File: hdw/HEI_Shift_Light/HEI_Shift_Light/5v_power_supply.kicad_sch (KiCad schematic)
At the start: 17 parts

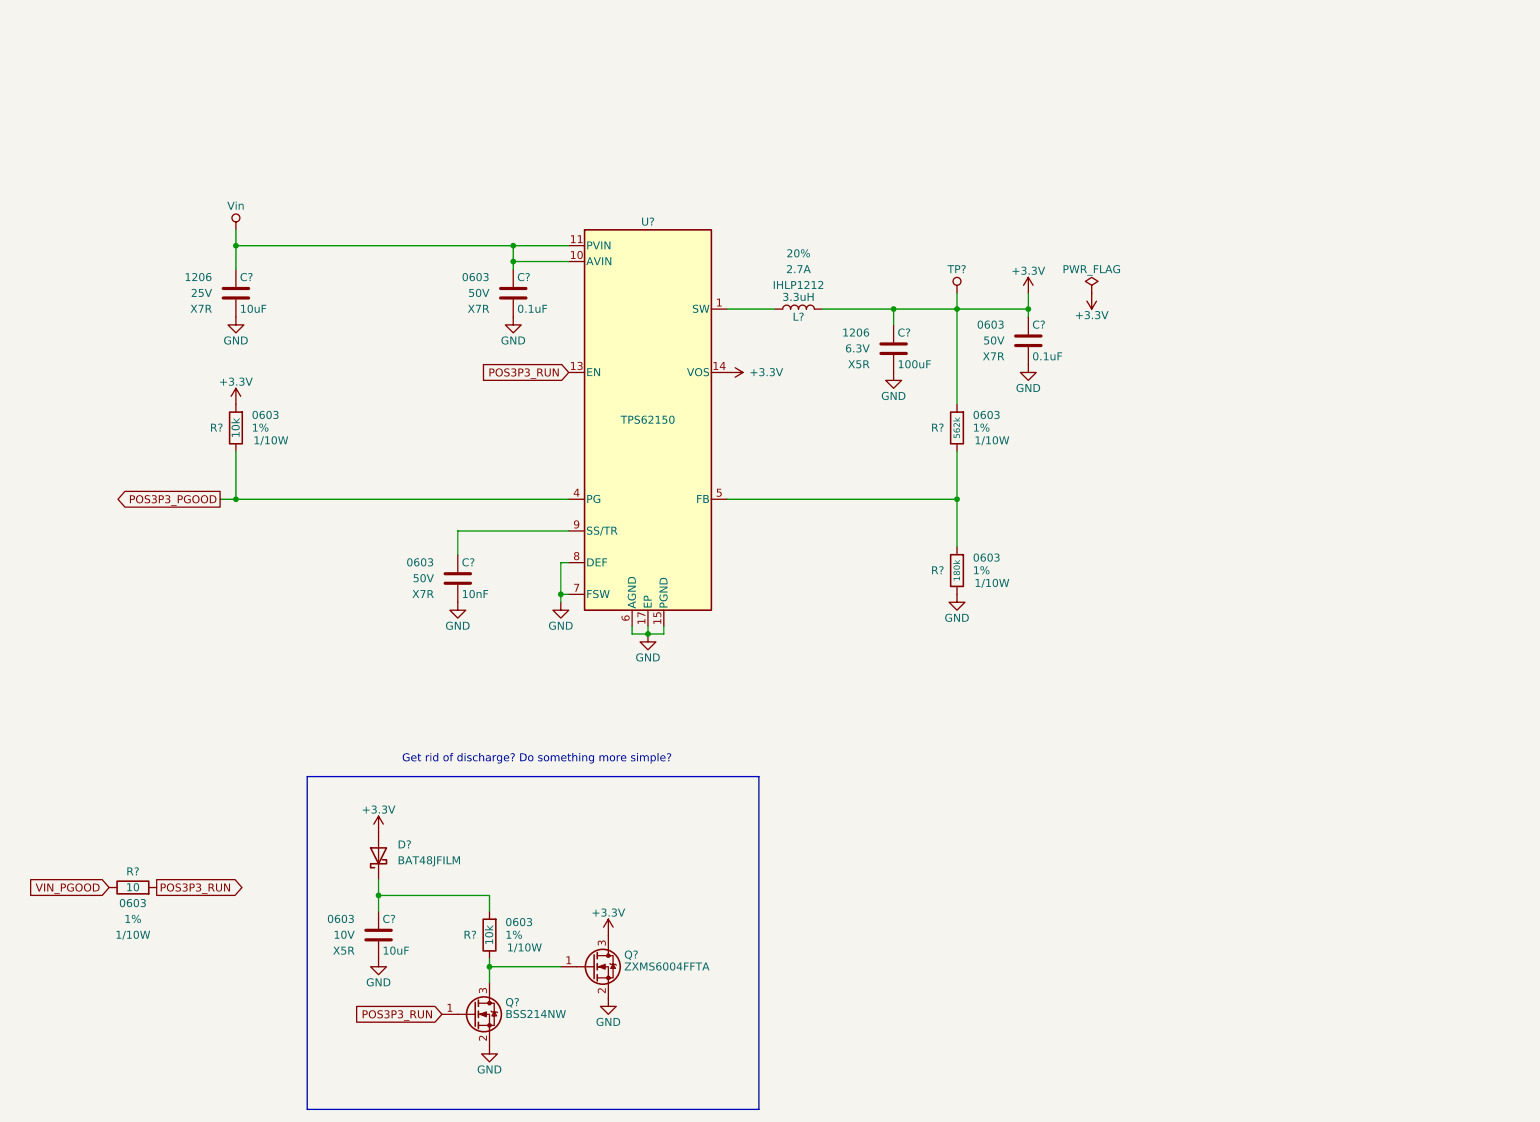
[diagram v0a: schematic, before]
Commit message: populated input protection circuit passive components, updated PIC pinout, added stuff to frequency to voltage converter circuit
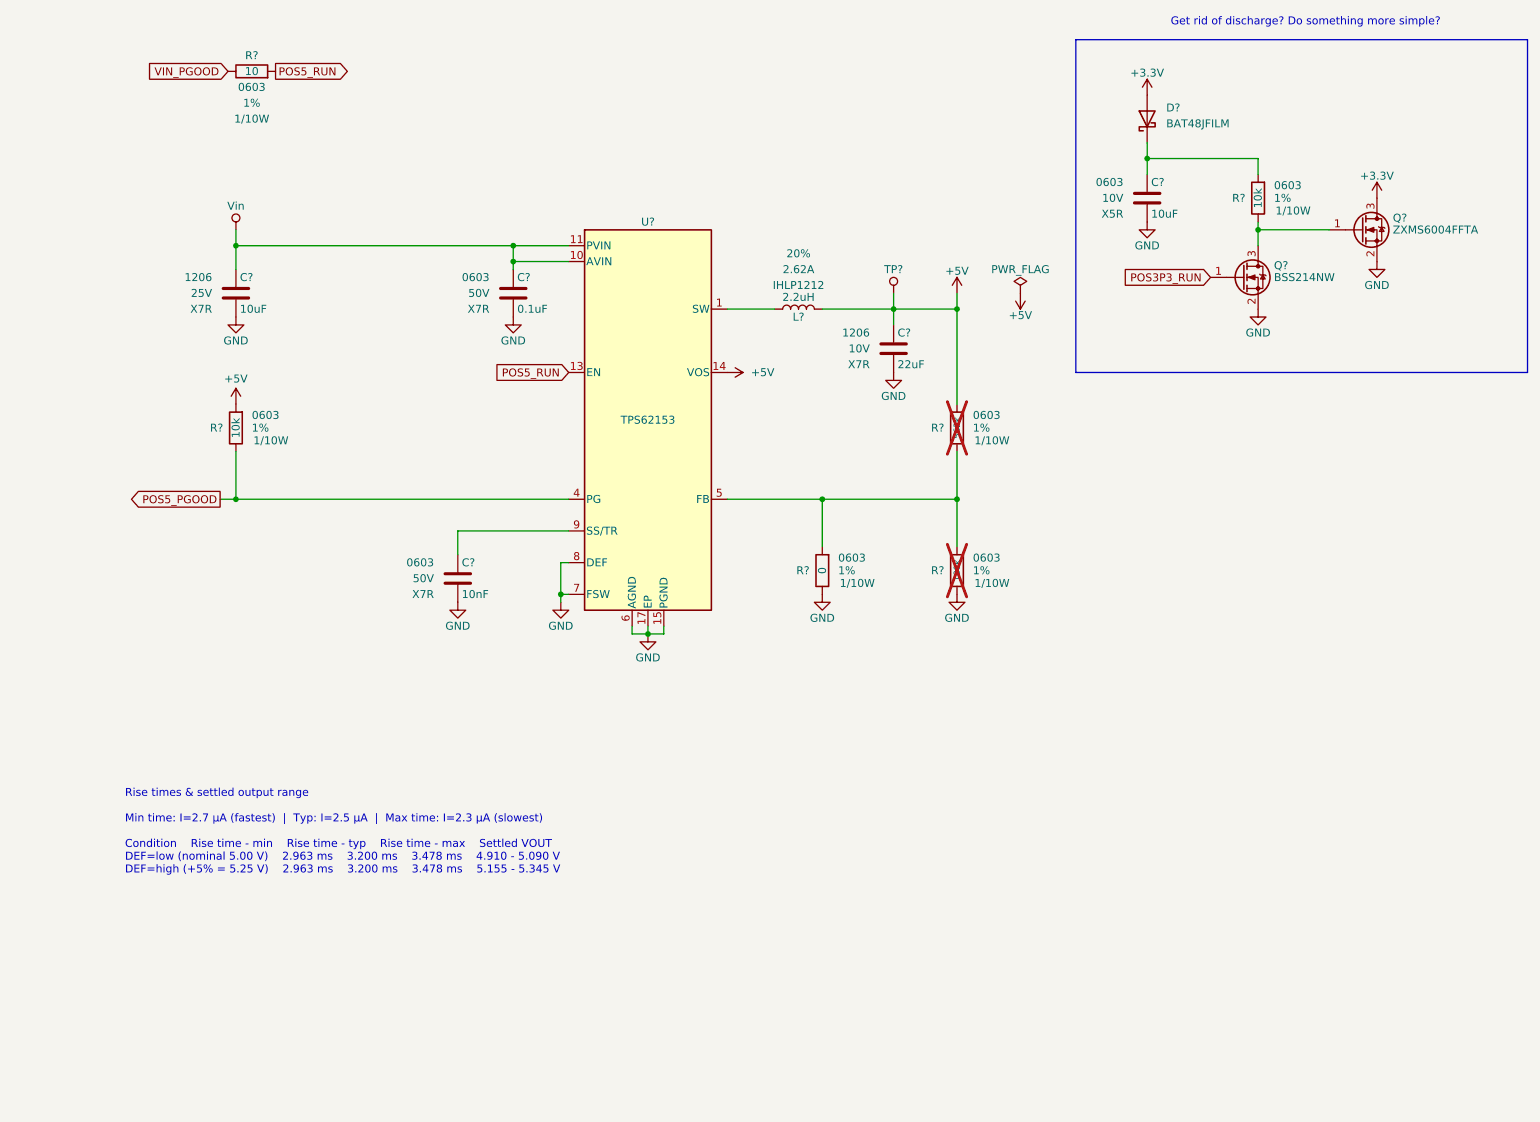
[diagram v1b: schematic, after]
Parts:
- removed C?: 0.1uF, Capacitors_SMD:C_0603, symbol Custom_Library:C_Custom
- added R?: 0, Resistors_SMD:R_0603, symbol Custom_Library:R_Custom
- C?: value 100uF -> 22uF; footprint Capacitors_SMD:C_1206 -> (none); Dielectric X5R -> X7R; Digi-Key PN 587-1963-1-ND -> (none); Voltage 6.3V -> 10V
- L?: value 3.3uH -> 2.2uH; Ampacity 2.7A -> 2.62A; Digi-Key PN 541-2567-1-ND -> 541-IHLP1212BZEV2R2M5ACT-ND
- R? (x2): now not fitted
- U?: value TPS62150 -> TPS62153; Digi-Key PN 296-41757-1-ND -> (none)
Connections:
- net +3.3V: no longer C?.1, L?.2, R?.1, R?.1, TP?.1 (TP), U?.14 (VOS)
- net GND: now also R?.2
- net POS3P3_RUN: no longer R?.1, U?.13 (EN)
- net at R?.1, R?.2, U?.5 (FB): now also R?.1
- net POS3P3_PGOOD renamed POS5_PGOOD
- new net +5V: C?.1, L?.2, R?.1, R?.1, TP?.1 (TP), U?.14 (VOS)
- new net POS5_RUN: R?.1, U?.13 (EN)
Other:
- note added: "Rise times & settled output range Min time: I=2.7 µA (fastest) | Typ: I=2.5 µA | Max time: I=2.3 µA (slowest) Condition Rise time - min Rise time - typ Rise time - max Settled VOUT DEF=low (nominal 5.00 V) 2.963 ms 3.200 ms 3.478 ms 4.910 - 5.090 V DEF=high (+5% = 5.25 V) 2.963 ms 3.200 ms 3.478 ms 5.155 - 5.345 V"
- moved on the sheet: C?, D?, Q?, R?, TP?

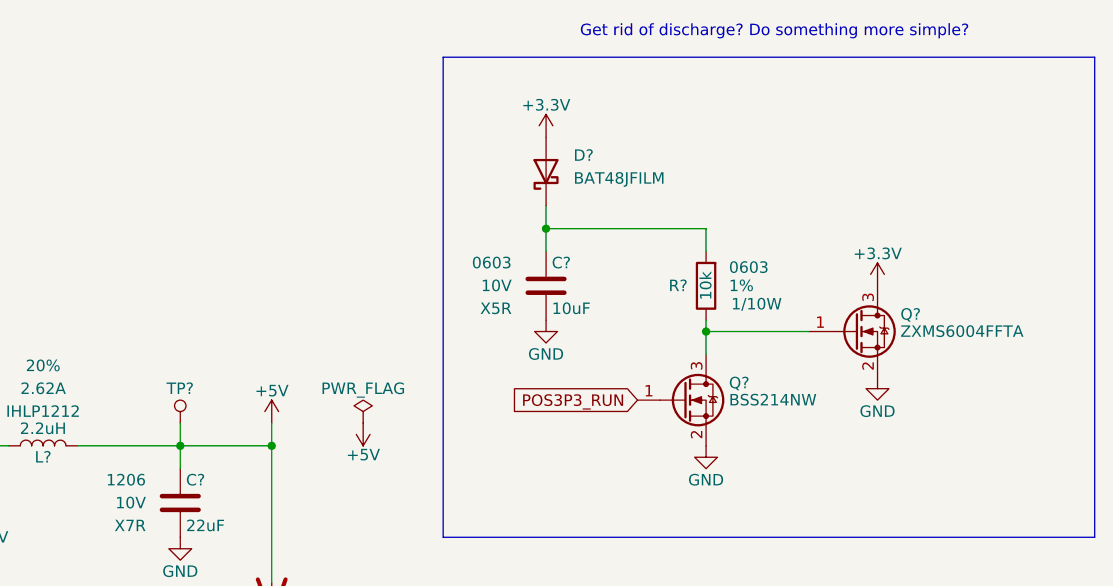
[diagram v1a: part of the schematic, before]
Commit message: added more shit, RGD LED, LC input filter
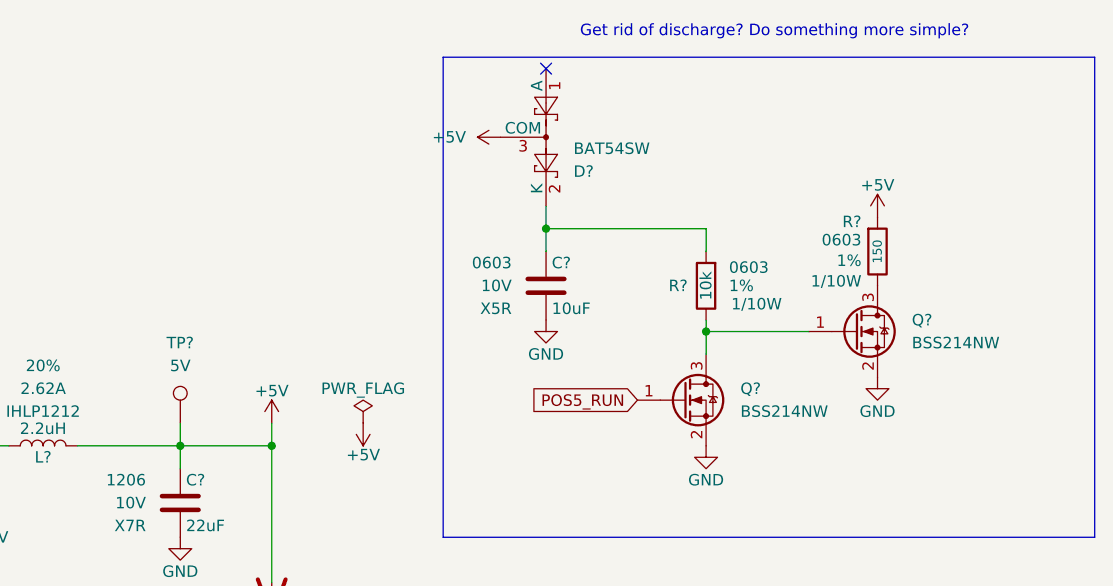
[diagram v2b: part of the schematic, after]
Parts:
- removed D?: BAT48JFILM, Diode_SMD:D_SOD-323, symbol Diode:BAT48JFILM
- removed Q?: BSS214NW, Package_TO_SOT_SMD:SOT-323_SC-70, symbol Transistor_FET:BSS214NW
- removed Q?: ZXMS6004FFTA, Package_TO_SOT_SMD:SOT-23, symbol Custom_Library:ZXMS6004FFTA
- removed TP?: TP, Custom Footprints Library:Test_Point, symbol Custom_Library:TP
- added D?: BAT54SW, Package_TO_SOT_SMD:SOT-323_SC-70, symbol Diode:BAT54SW
- added Q? (x2): BSS214NW, Package_TO_SOT_SMD:SOT-323_SC-70, symbol Transistor_FET:BSS214NW
- added R?: 150, symbol Custom_Library:R_Custom
- added TP?: 5V, TestPoint:TestPoint_Pad_D1.0mm, symbol Connector:TestPoint
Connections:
- net +5V: now also D?.3 (COM), R?.1, TP?.1
- net GND: now also Q?.2 (S), Q?.2 (S)
- net POS5_RUN: now also Q?.1 (G)
- net at R?.2: now also Q?.1 (G), Q?.3 (D)
- net at C?.1, R?.1: now also D?.2 (K)
- new net: Q?.3 (D), R?.2
- no-connect marks 0 -> 1
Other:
- company: (none) -> Drew Maatman
- title: (none) -> HEI Shift Light
